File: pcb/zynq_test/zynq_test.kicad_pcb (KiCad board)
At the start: 2 copper layers, 9 parts, among them J1101 RJ45_JK0654219, J701 1-1734248-5, J702 1-1734248-5, J703 1-1734248-5, U1 XC7Z020-2CLG400I, U1001 TUSB1210-Q1, U1003 AP22816AKBWT, U601 FT2232HQ, U903 TXS02612RTW

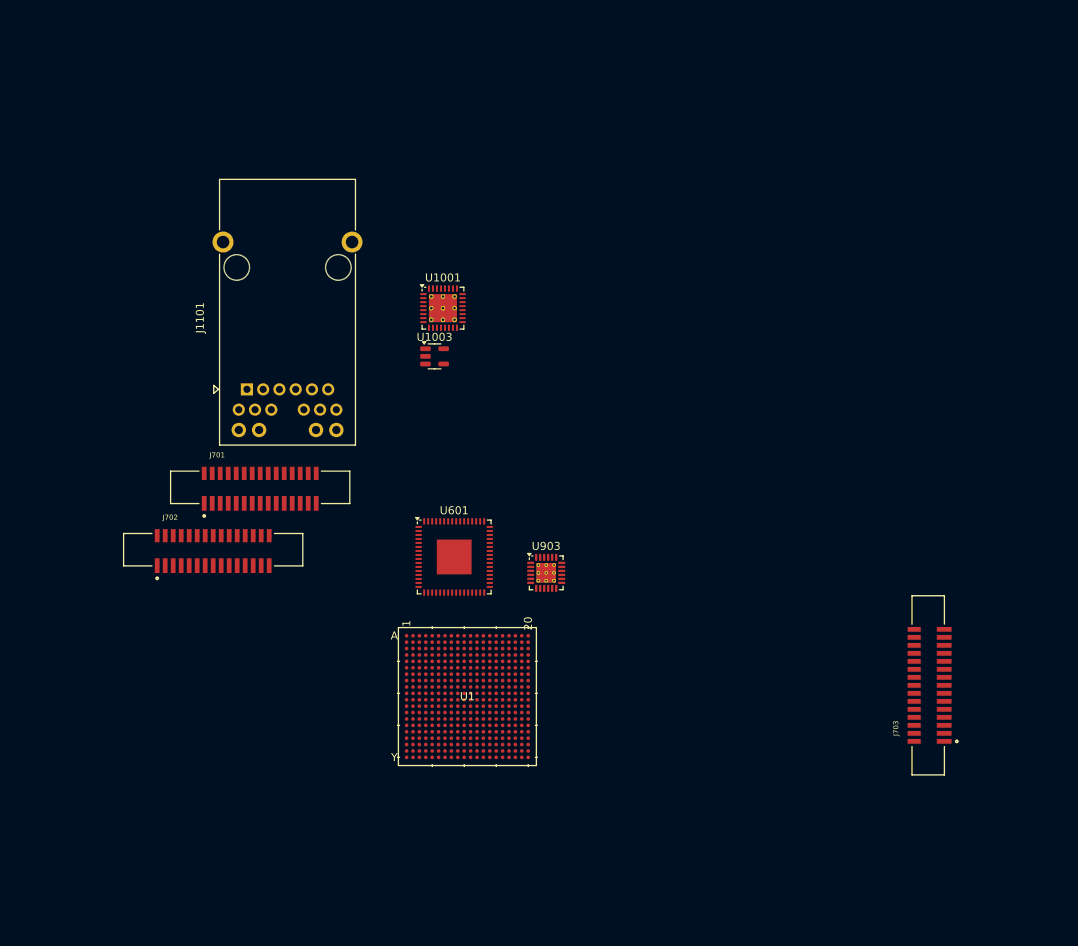
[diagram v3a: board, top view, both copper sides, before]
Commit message: Finished HDMI
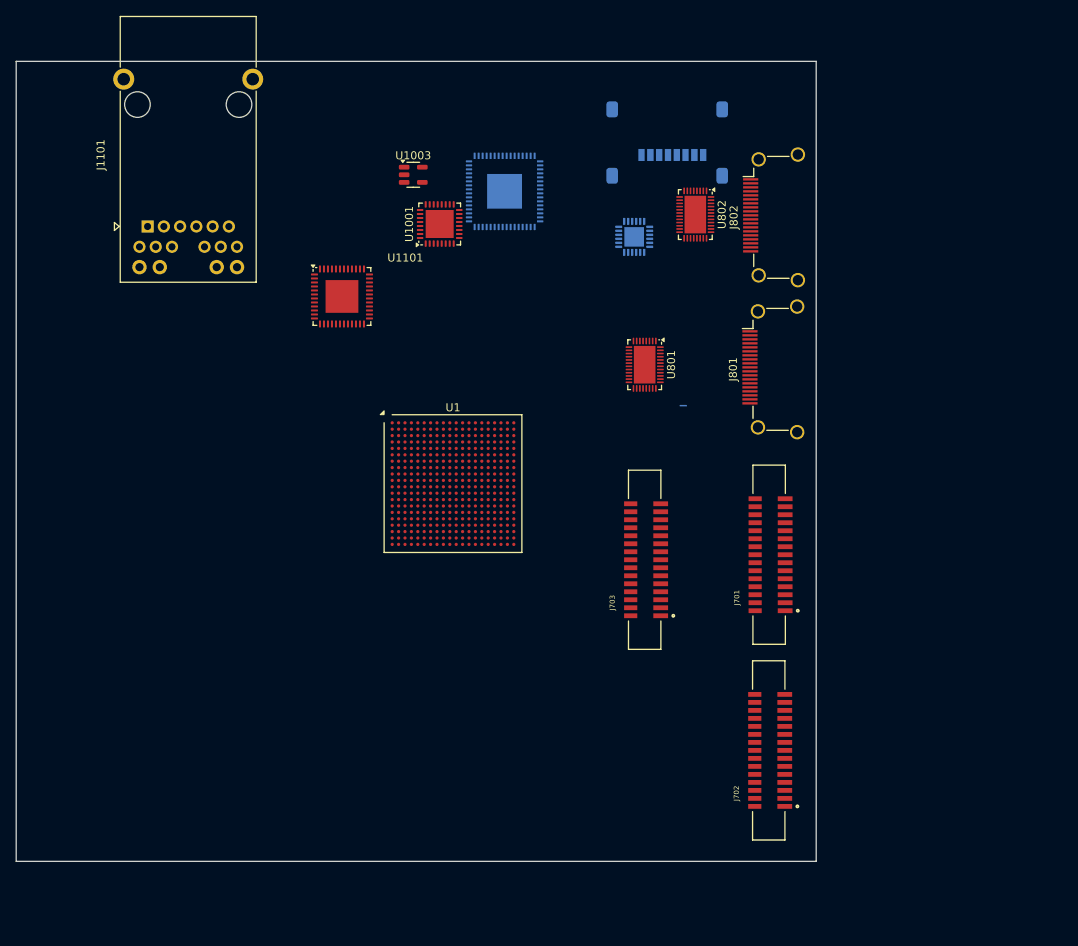
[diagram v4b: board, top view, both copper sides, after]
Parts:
- added J801: HDMI_A, Connector_Video:HDMI_A_Amphenol_10029449-x01xLF_Horizontal, F.Cu at (175.2, 78.5)
- added J802: HDMI_A, Connector_Video:HDMI_A_Amphenol_10029449-x01xLF_Horizontal, F.Cu at (175.3, 59.5)
- added J901: A-MicroTF-1.85A, Connector_Card:microSD_HC_Molex_47219-2001, B.Cu at (159.9, 49.6)
- added U1101: LAN8830, Package_DFN_QFN:VQFN-48-1EP_7x7mm_P0.5mm_EP4.1x4.1mm, F.Cu at (119.2, 69.4)
- added U801: TDP1204RNQR, Package_DFN_QFN:Texas_RNQ0040A_WQFN-40-1EP_6x4mm_P0.4mm_EP4.7x2.7mm, F.Cu at (157.1, 77.9)
- added U802: TDP1204RNQR, Package_DFN_QFN:Texas_RNQ0040A_WQFN-40-1EP_6x4mm_P0.4mm_EP4.7x2.7mm, F.Cu at (163.4, 59.2)
- U1: footprint Zynq:CLG400_ZYNQ-7000_AMD -> Package_BGA:Xilinx_CLG400
- U1001: footprint Package_DFN_QFN:VQFN-32-1EP_5x5mm_P0.5mm_EP3.5x3.5mm_ThermalVias -> Package_DFN_QFN:VQFN-32-1EP_5x5mm_P0.5mm_EP3.5x3.5mm
- U601: moved to B.Cu
- U903: footprint Package_DFN_QFN:WQFN-24-1EP_4x4mm_P0.5mm_EP2.45x2.45mm_ThermalVias -> Package_DFN_QFN:WQFN-24-1EP_4x4mm_P0.5mm_EP2.45x2.45mm; moved to B.Cu
- moved J702 73.8 mm to (172.5, 126.1), turned to 90 degrees
- moved J701 64.2 mm to (172.6, 101.7), turned to 90 degrees
- moved U601 46.1 mm to (139.6, 56.2), turned to 180 degrees
- moved U903 43.4 mm to (155.8, 61.9)
- moved J703 38.8 mm to (157.0, 102.3)
- moved U1 26.7 mm to (133.1, 92.8)
- moved J1101 23.8 mm to (94.9, 60.6)
- moved U1003 22.9 mm to (128.1, 54.2)
- moved U1001 10.5 mm to (131.4, 60.3), turned to 90 degrees
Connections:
- net Net-(J1101-MXCT1) renamed /ETHERNET/ETH_TX1_C
- net Net-(J1101-MXCT2) renamed /ETHERNET/ETH_TX2_C
- net Net-(J1101-MXCT3) renamed /ETHERNET/ETH_TX3_C
- net Net-(J1101-MXCT4) renamed /ETHERNET/ETH_TX4_C
- net Net-(J601-D+) renamed /Programmer/FTDI_D-
- net Net-(J601-D-) renamed /Programmer/FTDI_D+
- J1101 pad 10: Net-(J1101-MX1-) -> /ETHERNET/ETH_TX1_N
- J1101 pad 11: Net-(J1101-MX1+) -> /ETHERNET/ETH_TX1_P
- J1101 pad 2: Net-(J1101-MX3-) -> /ETHERNET/ETH_TX3_N
- J1101 pad 3: Net-(J1101-MX3+) -> /ETHERNET/ETH_TX3_P
- J1101 pad 4: Net-(J1101-MX2+) -> /ETHERNET/ETH_TX2_P
- J1101 pad 5: Net-(J1101-MX2-) -> /ETHERNET/ETH_TX2_N
- J1101 pad 8: Net-(J1101-MX4+) -> /ETHERNET/ETH_TX4_P
- J1101 pad 9: Net-(J1101-MX4-) -> /ETHERNET/ETH_TX4_N
- U1001 pad 11: unconnected-(U1001-CS-Pad11) -> +1V8
- U1001 pad 27: unconnected-(U1001-RESETB-Pad27) -> +1V8
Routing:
- net (no net): track 0.00 -> 0.75 mm
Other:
- board outline added: 100 x 100 mm

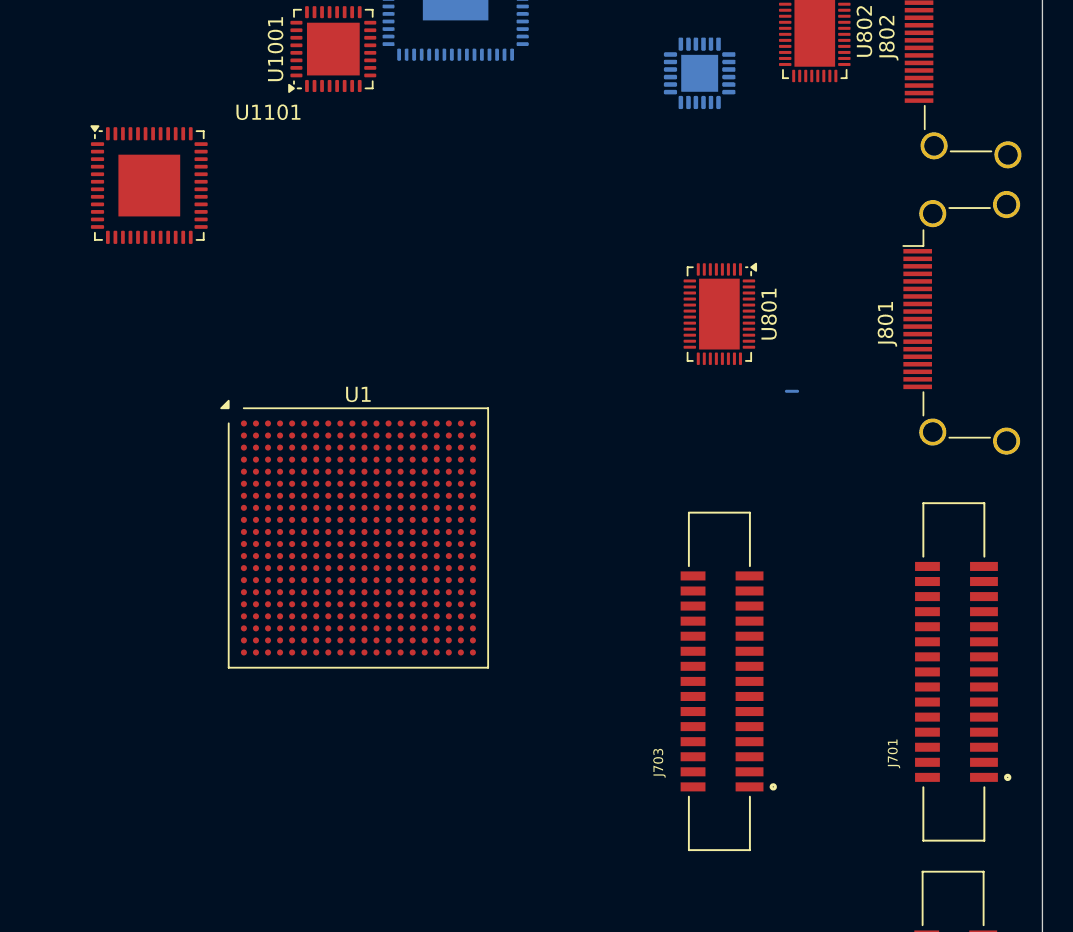
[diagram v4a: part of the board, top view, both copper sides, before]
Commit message: Started on DDR3
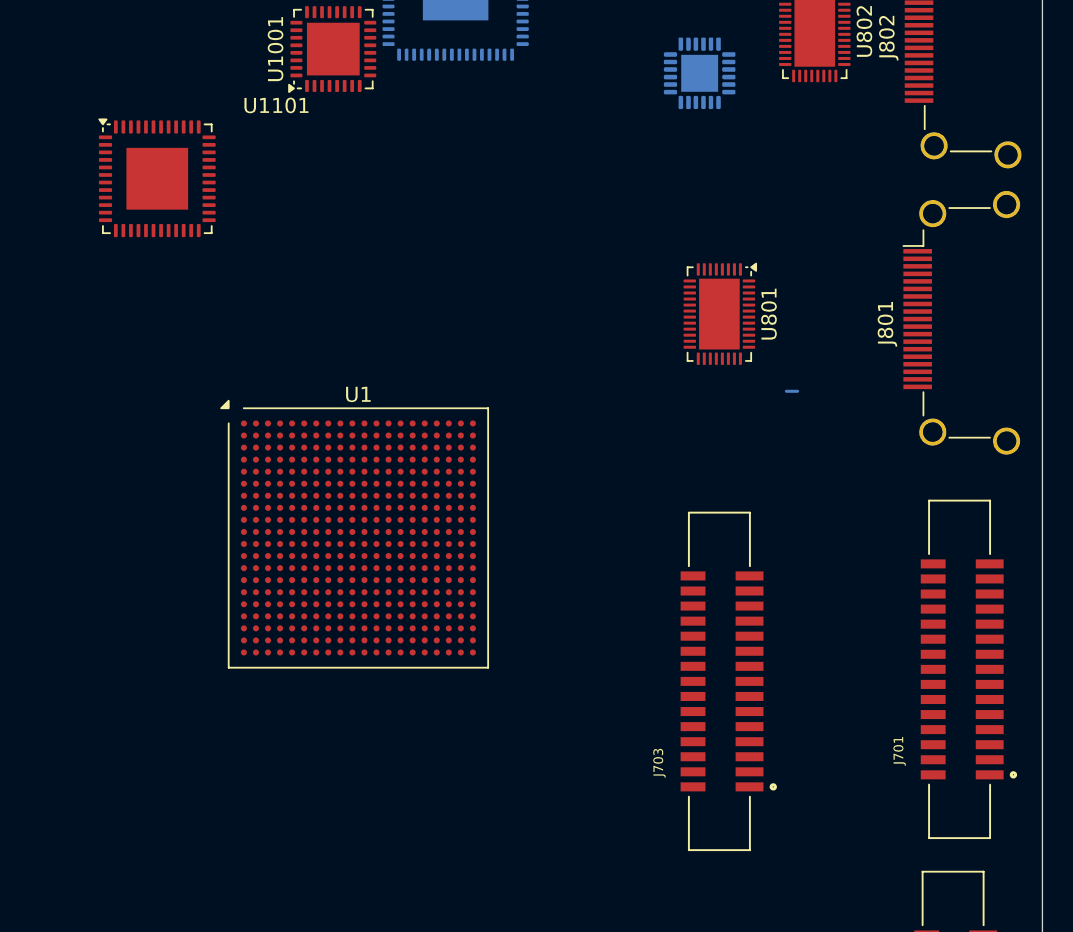
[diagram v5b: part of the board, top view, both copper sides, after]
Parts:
- moved U1101 0.70 mm to (119.8, 68.9)
- moved J701 0.42 mm to (173.0, 101.5)
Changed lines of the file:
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@@
 	(footprint "Camera:TE_1-1734248-5"
 		(layer "F.Cu")
-		(at 172.595 101.67 90)
+		(at 172.975 101.5 90)
 		(property "Reference" "J701"
 			(at -5.37339 -4.010418 90)
@@
 	(footprint "Package_DFN_QFN:VQFN-48-1EP_7x7mm_P0.5mm_EP4.1x4.1mm"
 		(layer "F.Cu")
-		(at 119.22 69.3875)
+		(at 119.75 68.9375)
 		(descr "VQFN, 48 Pin (http://www.ti.com/lit/ds/symlink/cc430f5137.pdf#page=128), generated with kicad-footprint-generator ipc_noLead_generator.py")
 		(tags "VQFN NoLead")

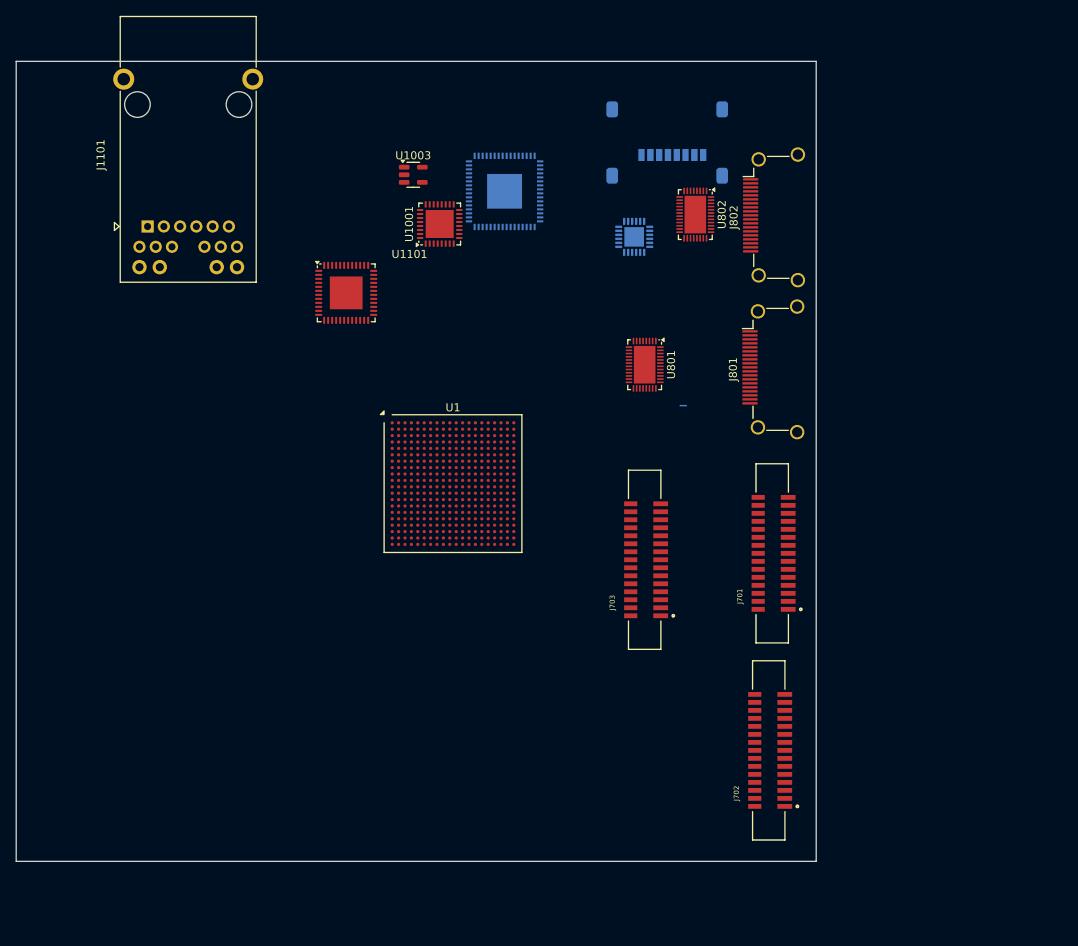
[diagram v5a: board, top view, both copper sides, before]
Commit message: Connected DDR3, cleaned up some thing
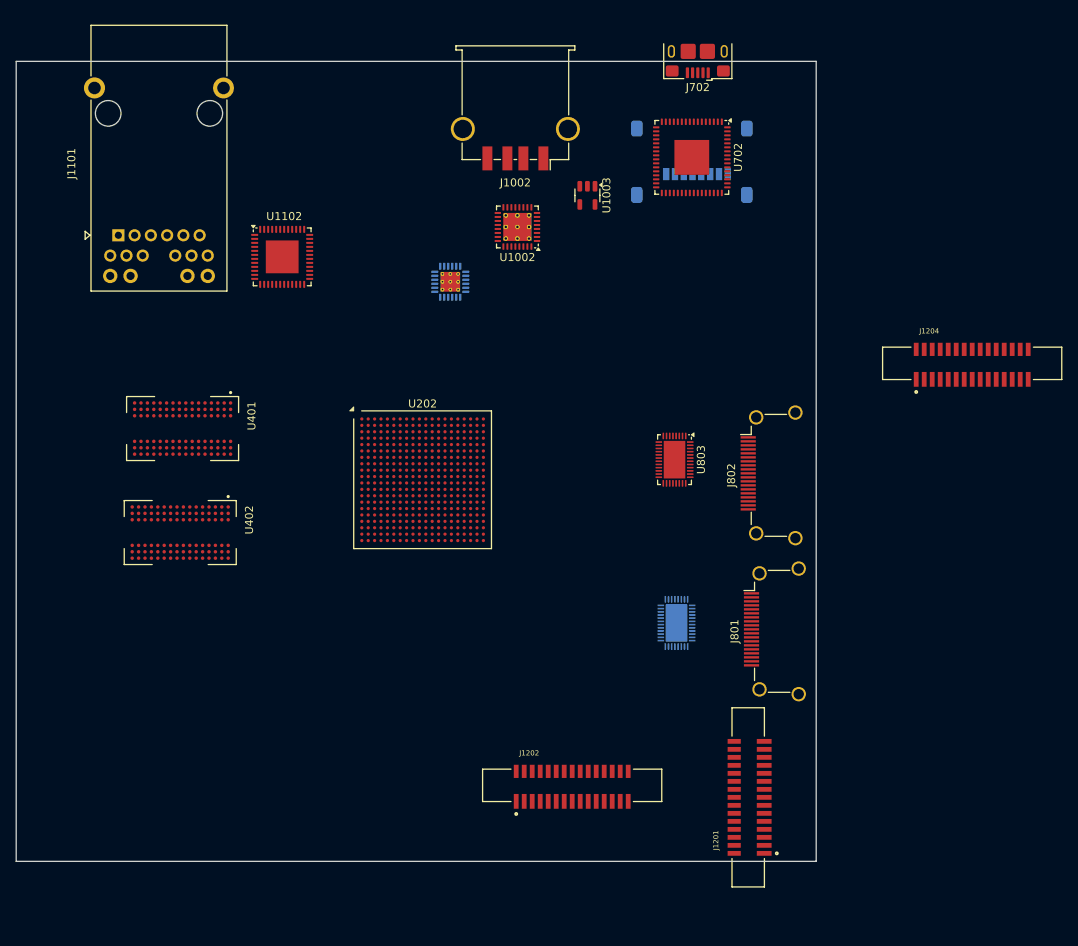
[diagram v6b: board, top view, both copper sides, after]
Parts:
- added J1002: USB_A, Connector_USB:USB_A_TE_292303-7_Horizontal, F.Cu at (140.9, 45.8)
- added J702: USB_B_Micro, Connector_USB:USB_Micro-B_Amphenol_10118193-0001LF_Horizontal, F.Cu at (163.7, 38.8)
- added U401: MT41K256M16TW-107, dram:BGA96C80P9X16_1400X800X120, F.Cu at (99.3, 85.9)
- added U402: MT41K256M16TW-107, dram:BGA96C80P9X16_1400X800X120, F.Cu at (99.0, 98.9)
- U1002: renamed from U1001; footprint Package_DFN_QFN:VQFN-32-1EP_5x5mm_P0.5mm_EP3.5x3.5mm -> Package_DFN_QFN:VQFN-32-1EP_5x5mm_P0.5mm_EP3.5x3.5mm_ThermalVias
- U702: renamed from U601; moved to F.Cu
- U806: renamed from U801; moved to B.Cu
- U901: renamed from U903; footprint Package_DFN_QFN:WQFN-24-1EP_4x4mm_P0.5mm_EP2.45x2.45mm -> Package_DFN_QFN:WQFN-24-1EP_4x4mm_P0.5mm_EP2.45x2.45mm_ThermalVias
- moved J1204 47.8 mm to (198.0, 77.7), turned to 0 degrees
- moved J801 32.8 mm to (175.4, 111.2)
- moved U806 32.5 mm to (161.0, 110.2)
- moved J802 32.3 mm to (175.0, 91.8)
- moved U803 30.7 mm to (160.8, 89.8)
- moved J1201 30.6 mm to (170.0, 132.0)
- moved J1202 24.9 mm to (148.0, 130.5), turned to 0 degrees
- moved U702 23.8 mm to (162.9, 52.0), turned to -90 degrees
- moved U901 23.7 mm to (132.8, 67.5)
- moved U1003 21.9 mm to (149.9, 56.8), turned to -90 degrees
- moved U1002 9.72 mm to (141.2, 60.7), turned to 180 degrees
- moved U1102 9.18 mm to (111.8, 64.4)
- moved J901 3.90 mm to (162.9, 52.0)
- moved U202 3.83 mm to (129.3, 92.3)
- moved J1101 3.82 mm to (91.3, 61.7)
- renumbered J701 to J1201, J702 to J1202, J703 to J1204, U1101 to U1102, U1 to U202, U802 to U803
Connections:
- net /Programmer/FTDI-CLK-12MHz renamed /Programmer/FTDI-CLK-12M
- net /ZynqPWR+JTAG/DONE renamed /Zynq PWR+JTAG/DONE
- net /ZynqPWR+JTAG/INIT renamed /Zynq PWR+JTAG/INIT
- net /ZynqPWR+JTAG/PROG renamed /Zynq PWR+JTAG/PROG
- net /ZynqPWR+JTAG/PS_RST renamed /Zynq PWR+JTAG/PS_RST
- net /ZynqPWR+JTAG/PWR_ON_RST renamed /Zynq PWR+JTAG/PWR_ON_RST
- net /ZynqPWR+JTAG/VCC_PLL renamed /Zynq PWR+JTAG/VCC+PLL
- net /ZynqPWR+JTAG/XADC_0 renamed /Zynq PWR+JTAG/XADC_0
- net /zynqMio/0.9_Vref renamed /Zynq Mio/0.9_Vref
- net /zynqMio/ETH0.RX-CLK renamed /ETHERNET/ETH0.RX-CLK
- net /zynqMio/ETH0.RX-CTL renamed /ETHERNET/ETH0.RX-CTL
- net /zynqMio/ETH0.RXD-0 renamed /ETHERNET/ETH0.RXD-0
- net /zynqMio/ETH0.RXD-1 renamed /ETHERNET/ETH0.RXD-1
- net /zynqMio/ETH0.RXD-2 renamed /ETHERNET/ETH0.RXD-2
- net /zynqMio/ETH0.RXD-3 renamed /ETHERNET/ETH0.RXD-3
- net /zynqMio/ETH0.TX-CLK.Z renamed /Zynq Mio/ETH0.TX-CLK.Z
- net /zynqMio/ETH0.TX-CTL.Z renamed /Zynq Mio/ETH0.TX-CTL.Z
- net /zynqMio/ETH0.TXD-0.Z renamed /Zynq Mio/ETH0.TXD-0.Z
- net /zynqMio/ETH0.TXD-1.Z renamed /Zynq Mio/ETH0.TXD-1.Z
- net /zynqMio/ETH0.TXD-2.Z renamed /Zynq Mio/ETH0.TXD-2.Z
- net /zynqMio/ETH0.TXD-3.Z renamed /Zynq Mio/ETH0.TXD-3.Z
- net /zynqMio/MIO0.0 renamed /Zynq Mio/MIO0.0
- net /zynqMio/MIO0.10 renamed /Zynq Mio/MIO0.10
- net /zynqMio/MIO0.11 renamed /Zynq Mio/MIO0.11
- net /zynqMio/MIO0.12 renamed /Zynq Mio/MIO0.12
- net /zynqMio/MIO0.13 renamed /Zynq Mio/MIO0.13
- net /zynqMio/MIO0.7 renamed /Zynq Mio/MIO0.7
- net /zynqMio/MIO0.8 renamed /Zynq Mio/MIO0.8
- net /zynqMio/MIO0.9 renamed /Zynq Mio/MIO0.9
- net /zynqMio/MIO1.46 renamed /Zynq Mio/MIO1.46
- net /zynqMio/MIO1.47 renamed /Zynq Mio/MIO1.47
- net /zynqMio/MIO1.48 renamed /Zynq Mio/MIO1.48
- net /zynqMio/MIO1.49 renamed /Zynq Mio/MIO1.49
- net /zynqMio/MIO1.50 renamed /Zynq Mio/MIO1.50
- net /zynqMio/MIO1.51 renamed /Zynq Mio/MIO1.51
- net /zynqMio/PS-CLK-33.33M renamed /Zynq Mio/PS-CLK-33.33M
- net /zynqMio/QSPI0.SCLK.Z renamed /Zynq Mio/QSPI0.SCLK.Z
- net /zynqMio/SD0.CLK.Z renamed /Zynq Mio/SD0.CLK.Z
- net /zynqMio/UART0.RX renamed /Programmer/UART0.RX
- net /zynqMio/UART0.TX renamed /Programmer/UART0.TX
- net Net-(C517-Pad1) renamed +1V35
- J1201 pad 10: GND -> unconnected-(J1201-Pad10)
- J1201 pad 10_1: GND -> unconnected-(J1201-10__1-Pad10_1)
- J1201 pad 11: /Cameras/CAM0.GPIO0 -> unconnected-(J1201-Pad11)
- J1201 pad 11_1: /Cameras/CAM0.GPIO0 -> unconnected-(J1201-11__1-Pad11_1)
- J1201 pad 12: /Cameras/CAM0.GPIO1 -> unconnected-(J1201-Pad12)
- J1201 pad 12_1: /Cameras/CAM0.GPIO1 -> unconnected-(J1201-12__1-Pad12_1)
- J1201 pad 13: /Cameras/CAM_RX.0.I2C_CLK -> unconnected-(J1201-Pad13)
- J1201 pad 13_1: /Cameras/CAM_RX.0.I2C_CLK -> unconnected-(J1201-13__1-Pad13_1)
- J1201 pad 14: /Cameras/CAM_RX.0.I2C_SDA -> unconnected-(J1201-Pad14)
- J1201 pad 14_1: /Cameras/CAM_RX.0.I2C_SDA -> unconnected-(J1201-14__1-Pad14_1)
- J1201 pad 15: +3.3V -> unconnected-(J1201-Pad15)
- J1201 pad 15_1: +3.3V -> unconnected-(J1201-15__1-Pad15_1)
- J1201 pad 1_1: GND -> /Cameras/CAM_RX.0.CAM_D0_N
- J1201 pad 2: /Cameras/CAM_RX.0.CAM_D0_N -> /Cameras/CAM_RX.0.CAM_D0_P
- J1201 pad 2_1: /Cameras/CAM_RX.0.CAM_D0_N -> GND
- J1201 pad 3: /Cameras/CAM_RX.0.CAM_D0_P -> /Cameras/CAM_RX.0.CAM_D1_N
- J1201 pad 3_1: /Cameras/CAM_RX.0.CAM_D0_P -> /Cameras/CAM_RX.0.CAM_D1_P
- J1201 pad 4_1: GND -> /Cameras/CAM_RX.0.CAM_CLK_N
- J1201 pad 5: /Cameras/CAM_RX.0.CAM_D1_N -> /Cameras/CAM_RX.0.CAM_CLK_P
- J1201 pad 5_1: /Cameras/CAM_RX.0.CAM_D1_N -> GND
- J1201 pad 6: /Cameras/CAM_RX.0.CAM_D1_P -> /Cameras/CAM0.GPIO0
- J1201 pad 6_1: /Cameras/CAM_RX.0.CAM_D1_P -> /Cameras/CAM0.GPIO1
- J1201 pad 7: GND -> /Cameras/CAM_RX.0.I2C_CLK
- J1201 pad 7_1: GND -> /Cameras/CAM_RX.0.I2C_SDA
- J1201 pad 8: /Cameras/CAM_RX.0.CAM_CLK_N -> +3.3V
- J1201 pad 8_1: /Cameras/CAM_RX.0.CAM_CLK_N -> unconnected-(J1201-8__1-Pad8_1)
- J1201 pad 9: /Cameras/CAM_RX.0.CAM_CLK_P -> unconnected-(J1201-Pad9)
- J1201 pad 9_1: /Cameras/CAM_RX.0.CAM_CLK_P -> unconnected-(J1201-9__1-Pad9_1)
- J1202 pad 10: GND -> unconnected-(J1202-Pad10)
- J1202 pad 10_1: GND -> unconnected-(J1202-10__1-Pad10_1)
- J1202 pad 11: /Cameras/CAM1.GPIO0 -> unconnected-(J1202-Pad11)
- J1202 pad 11_1: /Cameras/CAM1.GPIO0 -> unconnected-(J1202-11__1-Pad11_1)
- J1202 pad 12: /Cameras/CAM1.GPIO1 -> unconnected-(J1202-Pad12)
- J1202 pad 12_1: /Cameras/CAM1.GPIO1 -> unconnected-(J1202-12__1-Pad12_1)
- J1202 pad 13: /Cameras/CAM_RX.1.I2C_CLK -> unconnected-(J1202-Pad13)
- J1202 pad 13_1: /Cameras/CAM_RX.1.I2C_CLK -> unconnected-(J1202-13__1-Pad13_1)
- J1202 pad 14: /Cameras/CAM_RX.1.I2C_SDA -> unconnected-(J1202-Pad14)
- J1202 pad 14_1: /Cameras/CAM_RX.1.I2C_SDA -> unconnected-(J1202-14__1-Pad14_1)
- J1202 pad 15: +3.3V -> unconnected-(J1202-Pad15)
- J1202 pad 15_1: +3.3V -> unconnected-(J1202-15__1-Pad15_1)
- J1202 pad 1_1: GND -> /Cameras/CAM_RX.1.CAM_D0_N
- J1202 pad 2: /Cameras/CAM_RX.1.CAM_D0_N -> /Cameras/CAM_RX.1.CAM_D0_P
- J1202 pad 2_1: /Cameras/CAM_RX.1.CAM_D0_N -> GND
- J1202 pad 3: /Cameras/CAM_RX.1.CAM_D0_P -> /Cameras/CAM_RX.1.CAM_D1_N
- J1202 pad 3_1: /Cameras/CAM_RX.1.CAM_D0_P -> /Cameras/CAM_RX.1.CAM_D1_P
- J1202 pad 4_1: GND -> /Cameras/CAM_RX.1.CAM_CLK_N
- J1202 pad 5: /Cameras/CAM_RX.1.CAM_D1_N -> /Cameras/CAM_RX.1.CAM_CLK_P
- J1202 pad 5_1: /Cameras/CAM_RX.1.CAM_D1_N -> GND
- J1202 pad 6: /Cameras/CAM_RX.1.CAM_D1_P -> /Cameras/CAM1.GPIO0
- J1202 pad 6_1: /Cameras/CAM_RX.1.CAM_D1_P -> /Cameras/CAM1.GPIO1
- J1202 pad 7: GND -> /Cameras/CAM_RX.1.I2C_CLK
- J1202 pad 7_1: GND -> /Cameras/CAM_RX.1.I2C_SDA
- J1202 pad 8: /Cameras/CAM_RX.1.CAM_CLK_N -> +3.3V
- J1202 pad 8_1: /Cameras/CAM_RX.1.CAM_CLK_N -> unconnected-(J1202-8__1-Pad8_1)
- J1202 pad 9: /Cameras/CAM_RX.1.CAM_CLK_P -> unconnected-(J1202-Pad9)
- J1202 pad 9_1: /Cameras/CAM_RX.1.CAM_CLK_P -> unconnected-(J1202-9__1-Pad9_1)
- J1204 pad 10: GND -> unconnected-(J1204-Pad10)
- J1204 pad 10_1: GND -> unconnected-(J1204-10__1-Pad10_1)
- J1204 pad 11: /Cameras/CAM2.GPIO0 -> unconnected-(J1204-Pad11)
- J1204 pad 11_1: /Cameras/CAM2.GPIO0 -> unconnected-(J1204-11__1-Pad11_1)
- J1204 pad 12: /Cameras/CAM2.GPIO1 -> unconnected-(J1204-Pad12)
- J1204 pad 12_1: /Cameras/CAM2.GPIO1 -> unconnected-(J1204-12__1-Pad12_1)
- J1204 pad 13: /Cameras/CAM_TX.2.I2C_CLK -> unconnected-(J1204-Pad13)
- J1204 pad 13_1: /Cameras/CAM_TX.2.I2C_CLK -> unconnected-(J1204-13__1-Pad13_1)
- J1204 pad 14: /Cameras/CAM_TX.2.I2C_SDA -> unconnected-(J1204-Pad14)
- J1204 pad 14_1: /Cameras/CAM_TX.2.I2C_SDA -> unconnected-(J1204-14__1-Pad14_1)
- J1204 pad 15: +3.3V -> unconnected-(J1204-Pad15)
- J1204 pad 15_1: +3.3V -> unconnected-(J1204-15__1-Pad15_1)
- J1204 pad 1_1: GND -> /Cameras/CAM2.TX.0_N
- J1204 pad 2: /Cameras/CAM2.TX.0_N -> /Cameras/CAM2.TX.0_P
- J1204 pad 2_1: /Cameras/CAM2.TX.0_N -> GND
- J1204 pad 3: /Cameras/CAM2.TX.0_P -> /Cameras/CAM2.TX.1_N
- J1204 pad 3_1: /Cameras/CAM2.TX.0_P -> /Cameras/CAM2.TX.1_P
- J1204 pad 4_1: GND -> /Cameras/CAM2.TX.CLK_N
- J1204 pad 5: /Cameras/CAM2.TX.1_N -> /Cameras/CAM2.TX.CLK_P
- J1204 pad 5_1: /Cameras/CAM2.TX.1_N -> GND
- J1204 pad 6: /Cameras/CAM2.TX.1_P -> /Cameras/CAM2.GPIO0
- J1204 pad 6_1: /Cameras/CAM2.TX.1_P -> /Cameras/CAM2.GPIO1
- J1204 pad 7: GND -> /Cameras/CAM_TX.2.I2C_CLK
- J1204 pad 7_1: GND -> /Cameras/CAM_TX.2.I2C_SDA
- J1204 pad 8: /Cameras/CAM2.TX.CLK_N -> +3.3V
- J1204 pad 8_1: /Cameras/CAM2.TX.CLK_N -> unconnected-(J1204-8__1-Pad8_1)
- J1204 pad 9: /Cameras/CAM2.TX.CLK_P -> unconnected-(J1204-Pad9)
- J1204 pad 9_1: /Cameras/CAM2.TX.CLK_P -> unconnected-(J1204-9__1-Pad9_1)
- J801 pad 16: Net-(J801-SCL) -> Net-(J801-SDA)
- U1003 pad 3: +5V -> unconnected-(U1003-~{FLG}-Pad3)
- U1003 pad 5: +5V_{USB_OTG} -> +5V
- U202 pad A1: unconnected-(U1G-PS_DDR_DM0_502-PadA1) -> /Zynq Dram/DDR_L0.DM
- U202 pad A2: /ZynqDram/DDR_L0.2 -> /Zynq Dram/DDR_L0.2
- U202 pad A4: /ZynqDram/DDR_L0.3 -> /Zynq Dram/DDR_L0.3
- U202 pad B2: unconnected-(U1G-PS_DDR_DQS_N0_502-PadB2) -> /Zynq Dram/DDR_L0.DQS_N
- U202 pad B3: /ZynqDram/DDR_L0.1 -> /Zynq Dram/DDR_L0.1
- U202 pad B4: unconnected-(U1G-PS_DDR_DRST_B_502-PadB4) -> /Zynq Dram/DDR_CTR.RST
- U202 pad C1: /ZynqDram/DDR_L0.6 -> /Zynq Dram/DDR_L0.6
- U202 pad C10: /zynqMio/ETH0.MDC -> /ETHERNET/ETH0.MDC
- U202 pad C11: /zynqMio/ETH0.MDIO -> /ETHERNET/ETH0.MDIO
- U202 pad C2: unconnected-(U1G-PS_DDR_DQS_P0_502-PadC2) -> /Zynq Dram/DDR_L0.DQS_P
- U202 pad C3: /ZynqDram/DDR_L0.0 -> /Zynq Dram/DDR_L0.0
- U202 pad D1: /ZynqDram/DDR_L0.5 -> /Zynq Dram/DDR_L0.5
- U202 pad D3: /ZynqDram/DDR_L0.4 -> /Zynq Dram/DDR_L0.4
- U202 pad D4: unconnected-(U1G-PS_DDR_A13_502-PadD4) -> /Zynq Dram/DDR_ADDR13
- U202 pad E1: /ZynqDram/DDR_L0.7 -> /Zynq Dram/DDR_L0.7
- U202 pad E2: /ZynqDram/DDR_L0.8 -> /Zynq Dram/DDR_L1.8
- U202 pad E3: /ZynqDram/DDR_L1.9 -> /Zynq Dram/DDR_L1.9
- U202 pad E4: unconnected-(U1G-PS_DDR_A12_502-PadE4) -> /Zynq Dram/DDR_ADDR12
- U202 pad F1: unconnected-(U1G-PS_DDR_DM1_502-PadF1) -> /Zynq Dram/DDR_L1.DM
- U202 pad F2: unconnected-(U1G-PS_DDR_DQS_N1_502-PadF2) -> /Zynq Dram/DDR_L1.DQS_N
- U202 pad F4: unconnected-(U1G-PS_DDR_A14_502-PadF4) -> /Zynq Dram/DDR_ADDR14
- U202 pad F5: unconnected-(U1G-PS_DDR_A10_502-PadF5) -> /Zynq Dram/DDR_ADDR10
- U202 pad G2: unconnected-(U1G-PS_DDR_DQS_P1_502-PadG2) -> /Zynq Dram/DDR_L1.DQS_P
- U202 pad G3: /ZynqDram/DDR_L1.10 -> /Zynq Dram/DDR_L1.10
- U202 pad G4: unconnected-(U1G-PS_DDR_A11_502-PadG4) -> /Zynq Dram/DDR_ADDR11
- U202 pad G5: unconnected-(U1G-PS_DDR_VRN_502-PadG5) -> Net-(U202G-PS_DDR_VRN_502)
- U202 pad H1: /ZynqDram/DDR_L1.14 -> /Zynq Dram/DDR_L1.14
- U202 pad H2: /ZynqDram/DDR_L1.13 -> /Zynq Dram/DDR_L1.13
- U202 pad H3: /ZynqDram/DDR_L1.11 -> /Zynq Dram/DDR_L1.11
- U202 pad H5: unconnected-(U1G-PS_DDR_VRP_502-PadH5) -> Net-(U202G-PS_DDR_VRP_502)
- U202 pad H6: unconnected-(U1G-PS_DDR_VREF0_502-PadH6) -> V_{TT 0.675} REF
- U202 pad J1: /ZynqDram/DDR_L1.15 -> /Zynq Dram/DDR_L1.15
- U202 pad J3: /ZynqDram/DDR_L1.12 -> /Zynq Dram/DDR_L1.12
- U202 pad J4: unconnected-(U1G-PS_DDR_A9_502-PadJ4) -> /Zynq Dram/DDR_ADDR9
- U202 pad J5: unconnected-(U1G-PS_DDR_BA2_502-PadJ5) -> /Zynq Dram/DDR_CTR.BA2
- U202 pad K1: unconnected-(U1G-PS_DDR_A8_502-PadK1) -> /Zynq Dram/DDR_ADDR8
- U202 pad K2: unconnected-(U1G-PS_DDR_A1_502-PadK2) -> /Zynq Dram/DDR_ADDR1
- U202 pad K3: unconnected-(U1G-PS_DDR_A3_502-PadK3) -> /Zynq Dram/DDR_ADDR3
- U202 pad K4: unconnected-(U1G-PS_DDR_A7_502-PadK4) -> /Zynq Dram/DDR_ADDR7
- U202 pad L1: unconnected-(U1G-PS_DDR_A5_502-PadL1) -> /Zynq Dram/DDR_ADDR5
- U202 pad L2: unconnected-(U1G-PS_DDR_CKP_502-PadL2) -> /Zynq Dram/DDR_CTR.CLK_P
- U202 pad L4: unconnected-(U1G-PS_DDR_A6_502-PadL4) -> /Zynq Dram/DDR_ADDR6
- U202 pad L5: unconnected-(U1G-PS_DDR_BA0_502-PadL5) -> /Zynq Dram/DDR_CTR.BA0
- U202 pad M2: unconnected-(U1G-PS_DDR_CKN_502-PadM2) -> /Zynq Dram/DDR_CTR.CLK_N
- U202 pad M3: unconnected-(U1G-PS_DDR_A2_502-PadM3) -> /Zynq Dram/DDR_ADDR2
- U202 pad M4: unconnected-(U1G-PS_DDR_A4_502-PadM4) -> /Zynq Dram/DDR_ADDR4
- U202 pad M5: unconnected-(U1G-PS_DDR_WE_B_502-PadM5) -> /Zynq Dram/DDR_CTR.WE
- U202 pad N1: unconnected-(U1G-PS_DDR_CS_B_502-PadN1) -> /Zynq Dram/DDR_CTR.CS
- U202 pad N2: unconnected-(U1G-PS_DDR_A0_502-PadN2) -> /Zynq Dram/DDR_ADDR0
- U202 pad N3: unconnected-(U1G-PS_DDR_CKE_502-PadN3) -> /Zynq Dram/DDR_CTR.CLK_E
- U202 pad N5: unconnected-(U1G-PS_DDR_ODT_502-PadN5) -> /Zynq Dram/DDR_CTR.ODT
- U202 pad P1: /ZynqDram/DDR_L1.16 -> /Zynq Dram/DDR_L2.16
- U202 pad P3: /ZynqDram/DDR_L2.17 -> /Zynq Dram/DDR_L2.17
- U202 pad P4: unconnected-(U1G-PS_DDR_RAS_B_502-PadP4) -> /Zynq Dram/DDR_CTR.RAS
- U202 pad P5: unconnected-(U1G-PS_DDR_CAS_B_502-PadP5) -> /Zynq Dram/DDR_CTR.CAS
- U202 pad P6: unconnected-(U1G-PS_DDR_VREF1_502-PadP6) -> V_{TT 0.675} REF
- U202 pad R1: /ZynqDram/DDR_L2.19 -> /Zynq Dram/DDR_L2.19
- U202 pad R2: unconnected-(U1G-PS_DDR_DQS_P2_502-PadR2) -> /Zynq Dram/DDR_L2.DQS_P
- U202 pad R3: /ZynqDram/DDR_L2.18 -> /Zynq Dram/DDR_L2.18
- U202 pad R4: unconnected-(U1G-PS_DDR_BA1_502-PadR4) -> /Zynq Dram/DDR_CTR.BA1
- U202 pad T1: unconnected-(U1G-PS_DDR_DM2_502-PadT1) -> /Zynq Dram/DDR_L2.DM
- U202 pad T2: unconnected-(U1G-PS_DDR_DQS_N2_502-PadT2) -> /Zynq Dram/DDR_L2.DQS_N
- U202 pad T4: /ZynqDram/DDR_L2.20 -> /Zynq Dram/DDR_L2.20
- U202 pad U2: /ZynqDram/DDR_L2.22 -> /Zynq Dram/DDR_L2.22
- U202 pad U3: /ZynqDram/DDR_L2.23 -> /Zynq Dram/DDR_L2.23
- U202 pad U4: /ZynqDram/DDR_L2.21 -> /Zynq Dram/DDR_L2.21
- U202 pad V1: /ZynqDram/DDR_L3.24 -> /Zynq Dram/DDR_L3.24
- U202 pad V2: /ZynqDram/DDR_L3.30 -> /Zynq Dram/DDR_L3.30
- U202 pad V3: /ZynqDram/DDR_L3.31 -> /Zynq Dram/DDR_L3.31
- U202 pad W1: /ZynqDram/DDR_L3.26 -> /Zynq Dram/DDR_L3.26
- U202 pad W3: /ZynqDram/DDR_L3.29 -> /Zynq Dram/DDR_L3.29
- U202 pad W4: unconnected-(U1G-PS_DDR_DQS_N3_502-PadW4) -> /Zynq Dram/DDR_L3.DQS_P
- U202 pad W5: unconnected-(U1G-PS_DDR_DQS_P3_502-PadW5) -> /Zynq Dram/DDR_L3.DQS_N
- U202 pad Y1: unconnected-(U1G-PS_DDR_DM3_502-PadY1) -> /Zynq Dram/DDR_L3.DM
- U202 pad Y2: /ZynqDram/DDR_L3.28 -> /Zynq Dram/DDR_L3.28
- U202 pad Y3: /ZynqDram/DDR_L3.25 -> /Zynq Dram/DDR_L3.25
- U202 pad Y4: /ZynqDram/DDR_L3.27 -> /Zynq Dram/DDR_L3.27
- U702 pad 7: /Programmer/FTDI_D- -> /Programmer/FTDI_D+
- U702 pad 8: /Programmer/FTDI_D+ -> /Programmer/FTDI_D-
- U803 pad 11: /HDMI/HDMI.TX.HDP -> Net-(J802-HPD)
- U803 pad 32: Net-(J802-HPD) -> /HDMI/HDMI.TX.HDP
- U806 pad 10: Net-(J801-D2-) -> /HDMI/HDMI.RX.D2_N
- U806 pad 11: unconnected-(U801-HPD_OUT-Pad11) -> Net-(J801-HPD)
- U806 pad 12: Net-(J801-D1+) -> /HDMI/HDMI.RX.D1_P
- U806 pad 13: Net-(J801-D1-) -> /HDMI/HDMI.RX.D1_N
- U806 pad 15: Net-(J801-D0+) -> /HDMI/HDMI.RX.D0_P
- U806 pad 16: Net-(J801-D0-) -> /HDMI/HDMI.RX.D0_N
- U806 pad 18: Net-(J801-CK+) -> /HDMI/HDMI.RX.CLK_P
- U806 pad 19: Net-(J801-CK-) -> /HDMI/HDMI.RX.CLK_N
- U806 pad 26: Net-(J801-SCL) -> Net-(J801-SDA)
- U806 pad 30: /HDMI/HDMI.RX.CLK_N -> Net-(J801-CK-)
- U806 pad 31: /HDMI/HDMI.RX.CLK_P -> Net-(J801-CK+)
- U806 pad 32: Net-(J801-HPD) -> unconnected-(U806-HPD_IN-Pad32)
- U806 pad 33: /HDMI/HDMI.RX.D0_N -> Net-(J801-D0-)
- U806 pad 34: /HDMI/HDMI.RX.D0_P -> Net-(J801-D0+)
- U806 pad 36: /HDMI/HDMI.RX.D1_N -> Net-(J801-D1-)
- U806 pad 37: /HDMI/HDMI.RX.D1_P -> Net-(J801-D1+)
- U806 pad 39: /HDMI/HDMI.RX.D2_N -> Net-(J801-D2-)
- U806 pad 40: /HDMI/HDMI.RX.D2_P -> Net-(J801-D2+)
- U806 pad 9: Net-(J801-D2+) -> /HDMI/HDMI.RX.D2_P
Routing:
- net (no net): track 0.75 -> 0.00 mm
